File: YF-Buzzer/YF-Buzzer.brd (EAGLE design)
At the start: 100 x 100 mm, 40 parts, among them IC1 74HC595N, IC2 74HC595N, IC3 74HC595N, IC4 74HC595N, IC5 74HC595N, IC6 74HC595N, IC7 74150N

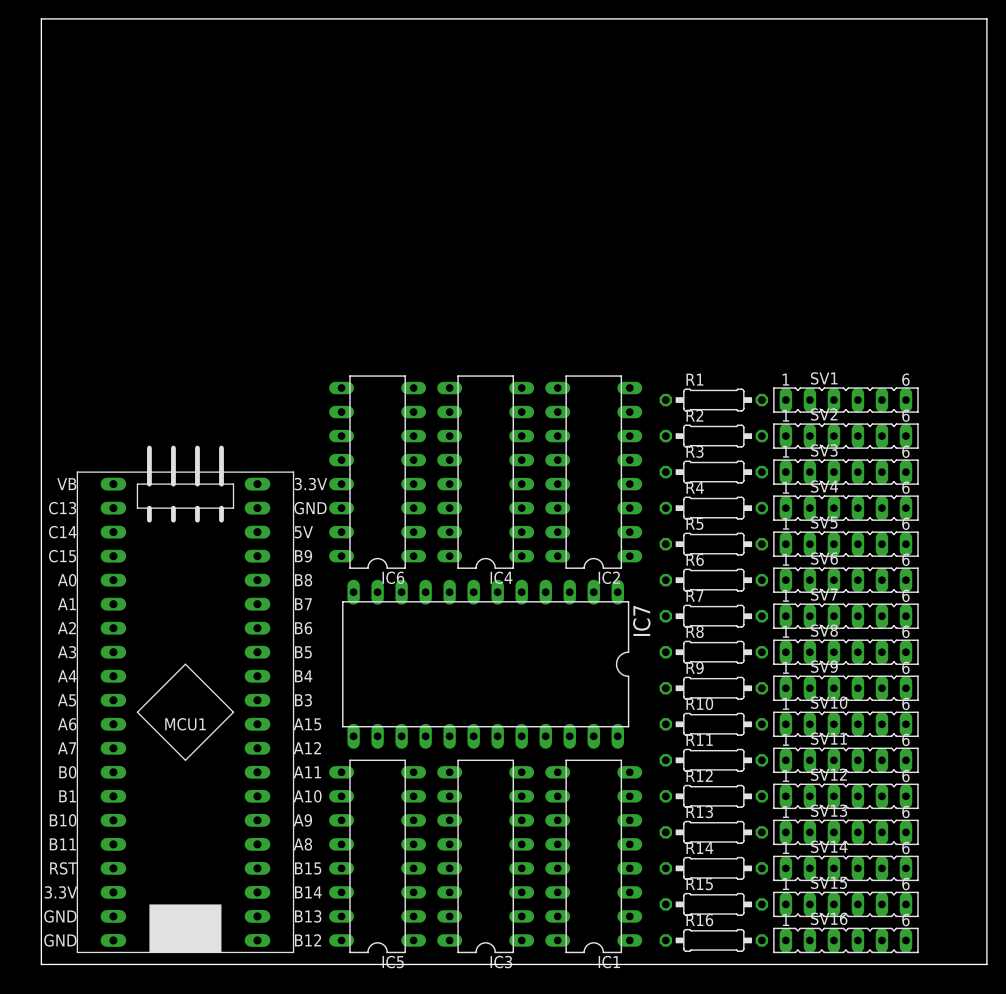
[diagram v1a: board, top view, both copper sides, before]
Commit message: Autorouted the rest of the main circuit.
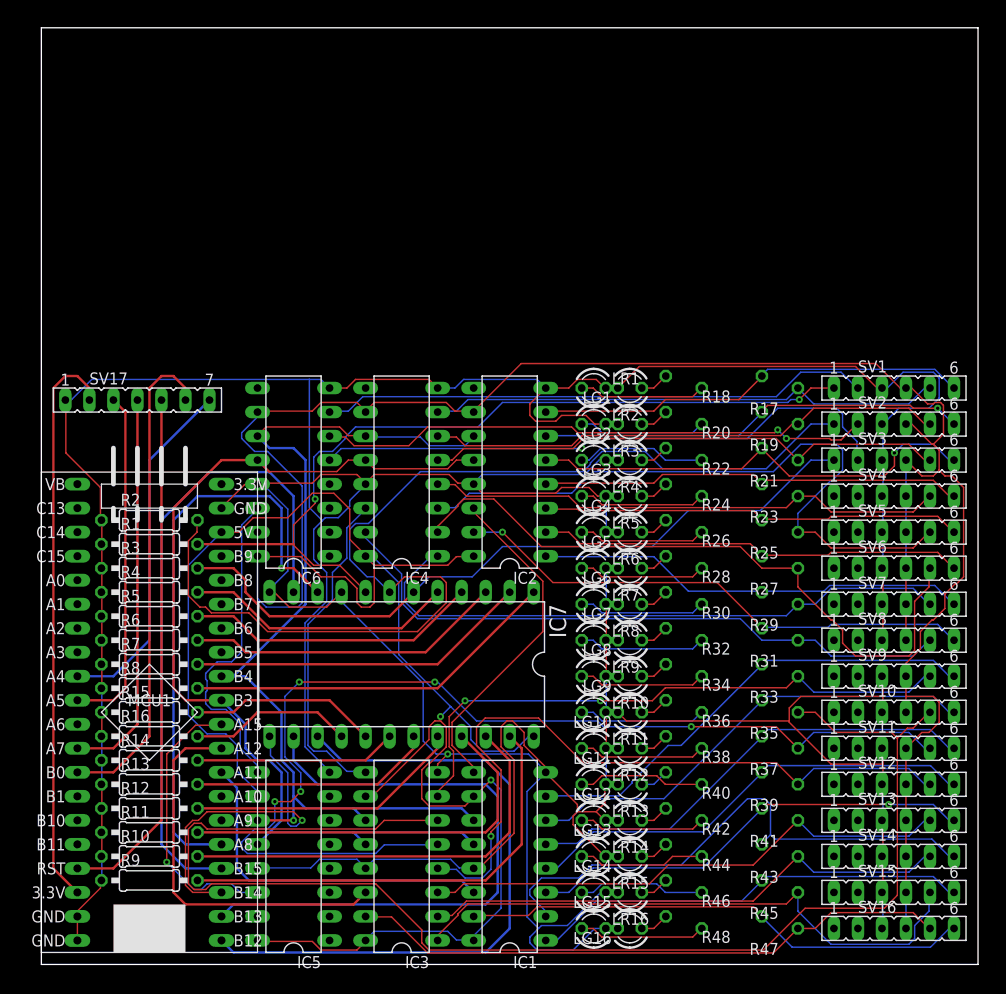
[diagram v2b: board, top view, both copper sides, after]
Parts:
- added LG1, LG10, LG11, LG12, LG13, LG14, LG15, LG16, LG2, LG3, LG4, LG5, LG6, LG7, LG8, LG9, LR1, LR10, LR11, LR12, LR13, LR14, LR15, LR16, LR2, LR3, LR4, LR5, LR6, LR7, LR8, LR9: (no value), led:LED3MM
- added R17, R18, R19, R20, R21, R22, R23, R24, R25, R26, R27, R28, R29, R30, R31, R32, R33, R34, R35, R36, R37, R38, R39, R40, R41, R42, R43, R44, R45, R46, R47, R48: (no value), rcl:0207/10
- added SV17: (no value), con-lsta:FE07
- moved R16 63.5 mm to (11.4, 24.1)
- moved R15 63.1 mm to (11.4, 26.7)
- moved R9 63.1 mm to (11.4, 8.89)
- moved R1 61.6 mm to (11.4, 44.5)
- moved R10 61.3 mm to (11.4, 11.4)
- moved R14 60.8 mm to (11.4, 21.6)
- moved R3 60.5 mm to (11.4, 41.9)
- moved R2 60.3 mm to (11.4, 47.0)
- moved R4 60.3 mm to (11.4, 39.4)
- moved R11 60.2 mm to (11.4, 14.0)
- moved R5 60.2 mm to (11.4, 36.8)
- moved R6 60.0 mm to (11.4, 34.3)
- moved R13 59.9 mm to (11.4, 19.1)
- moved R7 59.9 mm to (11.4, 31.8)
- moved R8 59.8 mm to (11.4, 29.2)
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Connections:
- removed net 3.3V1: MCU1.3.3V1
- new net LCD_CLK: MCU1.A5, SV17.3
- new net LCD_CS: MCU1.A4, SV17.7
- new net LCD_DATA: MCU1.A7, SV17.4
- new net LCD_DC: MCU1.B0, SV17.6
- new net LCD_RST: MCU1.R, SV17.5
- new net N$10: LG2.A, R20.1
- new net N$101: LR14.A, R43.1
- new net N$102: LG14.A, R44.1
- new net N$105: SV14.2
- new net N$106: SV14.1
- new net N$113: LR15.A, R45.1
- new net N$114: LG15.A, R46.1
- new net N$117: SV15.2
- new net N$118: SV15.1
- new net N$125: LR16.A, R47.1
- new net N$126: LG16.A, R48.1
- new net N$129: SV16.2
- new net N$130: SV16.1
- new net N$137: LR1.A, R17.1
- new net N$138: LG1.A, R18.1
- new net N$15: LR3.A, R21.1
- new net N$17: LG3.A, R22.1
- new net N$22: LR5.A, R25.1
- new net N$23: LG5.A, R26.1
- new net N$26: SV5.2
- new net N$27: SV5.1
- new net N$28: LR4.A, R23.1
- new net N$29: LG4.A, R24.1
- new net N$32: SV4.2
- new net N$33: SV4.1
- new net N$34: LR6.A, R27.1
- new net N$35: LG6.A, R28.1
- new net N$36: MCU1.3.3V1, SV17.2
- new net N$39: SV6.2
- new net N$40: SV6.1
- new net N$41: LR7.A, R29.1
- new net N$42: LG7.A, R30.1
- new net N$45: SV7.2
- new net N$46: SV7.1
- new net N$47: LR8.A, R31.1
- new net N$48: LG8.A, R32.1
- new net N$51: SV8.2
- new net N$52: SV8.1
- new net N$53: LR9.A, R33.1
- new net N$54: LG9.A, R34.1
- new net N$57: SV9.2
- new net N$58: SV9.1
- new net N$59: LR11.A, R37.1
- new net N$60: LG11.A, R38.1
- new net N$63: SV11.2
- new net N$64: SV11.1
- new net N$71: LR12.A, R39.1
- new net N$72: LG12.A, R40.1
- new net N$73: LR10.A, R35.1
- new net N$74: LG10.A, R36.1
- new net N$77: SV10.2
- new net N$78: SV10.1
- new net N$81: SV12.2
- new net N$82: SV12.1
- new net N$89: LR13.A, R41.1
- new net N$9: LR2.A, R19.1
- new net N$90: LG13.A, R42.1
- new net N$93: SV13.2
- new net N$94: SV13.1
- net IN10: no longer SV11.1
- net IN11: no longer SV12.1
- net IN12: no longer SV13.1
- net IN13: no longer SV14.1
- net IN14: no longer SV15.1
- net IN15: no longer SV16.1
- net IN3: no longer SV4.1
- net IN4: no longer SV5.1
- net IN5: no longer SV6.1
- net IN6: no longer SV7.1
- net IN7: no longer SV8.1
- net IN8: no longer SV9.1
- net IN9: no longer SV10.1
- net LG0: now also R18.2
- net LG1: now also R20.2
- net LG10: now also R38.2
- net LG11: now also R40.2
- net LG12: now also R42.2
- net LG13: now also R44.2
- net LG14: now also R46.2
- net LG15: now also R48.2
- net LG2: now also R22.2
- net LG3: now also R24.2
- net LG4: now also R26.2
- net LG5: now also R28.2
- net LG6: now also R30.2
- net LG7: now also R32.2
- net LG8: now also R34.2
- net LG9: now also R36.2
- net LR0: now also R17.2
- net LR1: now also R19.2
- net LR10: now also R37.2
- net LR11: now also R39.2
- net LR12: now also R41.2
- net LR13: now also R43.2
- net LR14: now also R45.2
- net LR15: now also R47.2
- net LR2: now also R21.2
- net LR3: now also R23.2
- net LR4: now also R25.2
- net LR5: now also R27.2
- net LR6: now also R29.2
- net LR7: now also R31.2
- net LR8: now also R33.2
- net LR9: now also R35.2
- net LY10: no longer SV11.2
- net LY11: no longer SV12.2
- net LY12: no longer SV13.2
- net LY13: no longer SV14.2
- net LY14: no longer SV15.2
- net LY15: no longer SV16.2
- net LY3: no longer SV4.2
- net LY4: no longer SV5.2
- net LY5: no longer SV6.2
- net LY6: no longer SV7.2
- net LY7: no longer SV8.2
- net LY8: no longer SV9.2
- net LY9: no longer SV10.2
- net PE: now also LG1.K, LG10.K, LG11.K, LG12.K, LG13.K, LG14.K, LG15.K, LG16.K, LG2.K, LG3.K, LG4.K, LG5.K, LG6.K, LG7.K, LG8.K, LG9.K, LR1.K, LR10.K, LR11.K, LR12.K, LR13.K, LR14.K, LR15.K, LR16.K, LR2.K, LR3.K, LR4.K, LR5.K, LR6.K, LR7.K, LR8.K, LR9.K, SV17.1
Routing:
- net PE: track 0.00 -> 594.3 mm, vias 0 -> 1
- net +5V: track 0.00 -> 401.9 mm, vias 0 -> 2
- net LR9: track 0.00 -> 147.5 mm
- net LR10: track 0.00 -> 115.6 mm, vias 0 -> 5
- net IN1: track 0.00 -> 113.8 mm
- net LATCH: track 0.00 -> 103.9 mm
- net CLK: track 0.00 -> 103.7 mm, vias 0 -> 1
- net IN0: track 0.00 -> 88.3 mm, vias 0 -> 2
- net IN2: track 0.00 -> 77.0 mm
- net LR11: track 0.00 -> 75.7 mm, vias 0 -> 1
- net LR4: track 0.00 -> 72.0 mm
- net LR5: track 0.00 -> 70.9 mm
- net MUX_A: track 0.00 -> 69.7 mm
- net MUX_D: track 0.00 -> 69.0 mm
- net LR7: track 0.00 -> 68.0 mm
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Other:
- board size 100 x 100 mm -> 99.1 x 99.1 mm

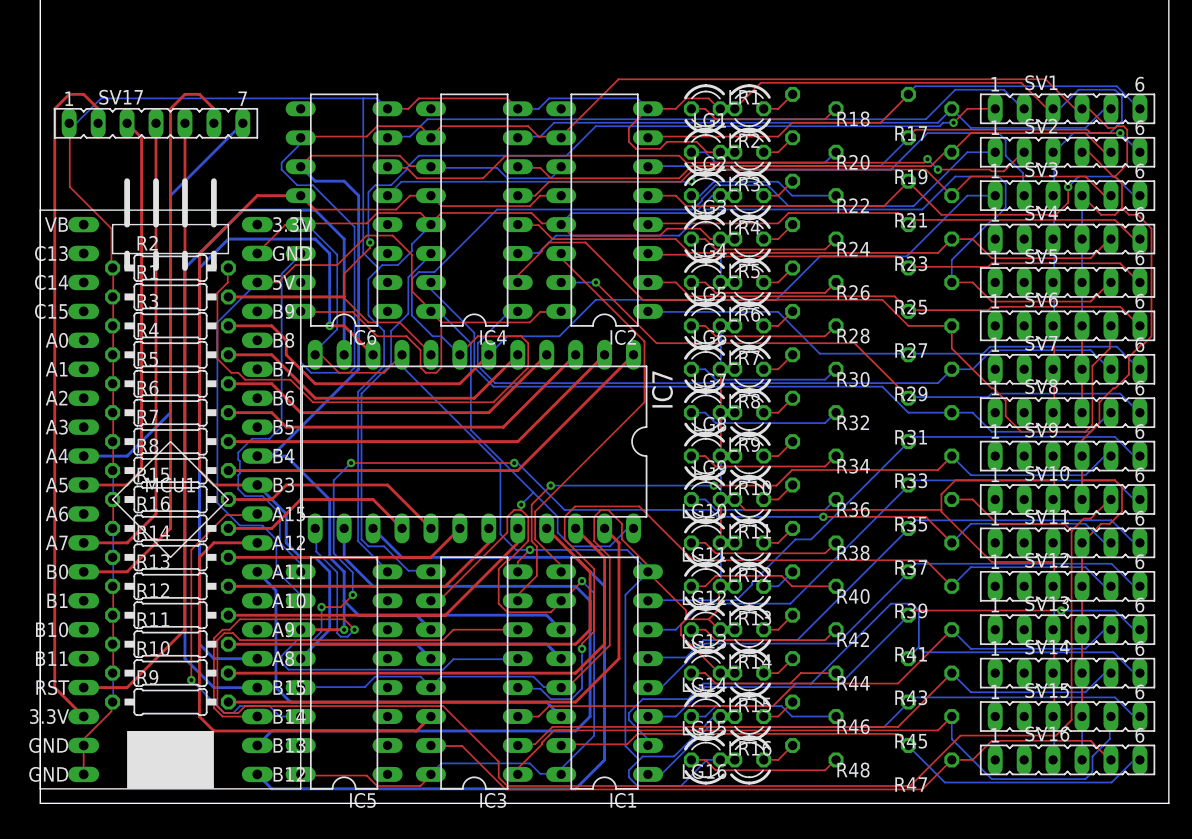
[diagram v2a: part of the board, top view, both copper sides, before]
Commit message: Removed LED's and cleaned up the circuit.
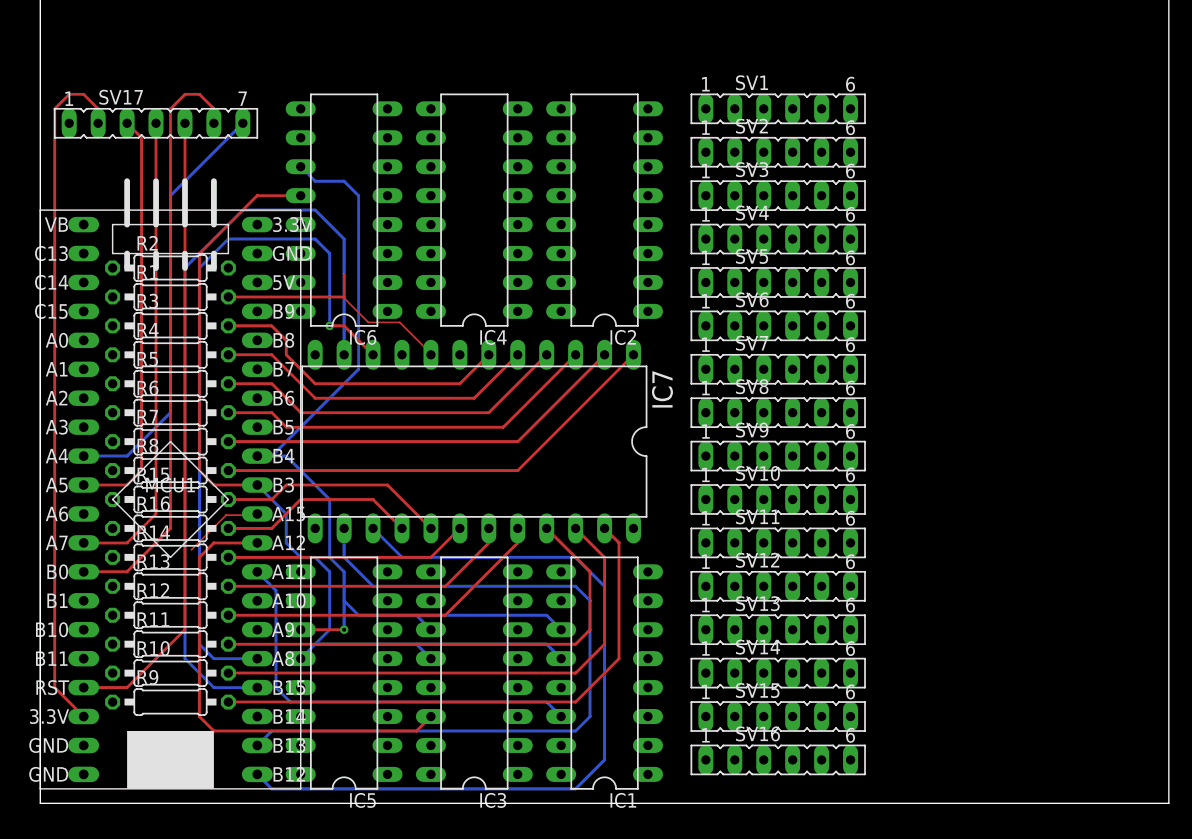
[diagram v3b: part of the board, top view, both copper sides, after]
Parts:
- removed LG1, LG10, LG11, LG12, LG13, LG14, LG15, LG16, LG2, LG3, LG4, LG5, LG6, LG7, LG8, LG9, LR1, LR10, LR11, LR12, LR13, LR14, LR15, LR16, LR2, LR3, LR4, LR5, LR6, LR7, LR8, LR9: (no value), led:LED3MM
- removed R17, R18, R19, R20, R21, R22, R23, R24, R25, R26, R27, R28, R29, R30, R31, R32, R33, R34, R35, R36, R37, R38, R39, R40, R41, R42, R43, R44, R45, R46, R47, R48: (no value), rcl:0207/10
- moved SV1 25.4 mm to (64.8, 61.0)
- moved SV10 25.4 mm to (64.8, 26.7)
- moved SV11 25.4 mm to (64.8, 22.9)
- moved SV12 25.4 mm to (64.8, 19.1)
- moved SV13 25.4 mm to (64.8, 15.2)
- moved SV14 25.4 mm to (64.8, 11.4)
- moved SV15 25.4 mm to (64.8, 7.62)
- moved SV16 25.4 mm to (64.8, 3.81)
- moved SV2 25.4 mm to (64.8, 57.1)
- moved SV3 25.4 mm to (64.8, 53.3)
- moved SV4 25.4 mm to (64.8, 49.5)
- moved SV5 25.4 mm to (64.8, 45.7)
- moved SV6 25.4 mm to (64.8, 41.9)
- moved SV7 25.4 mm to (64.8, 38.1)
- moved SV8 25.4 mm to (64.8, 34.3)
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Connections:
- removed net N$10: LG2.A, R20.1
- removed net N$101: LR14.A, R43.1
- removed net N$102: LG14.A, R44.1
- removed net N$105: SV14.2
- removed net N$106: SV14.1
- removed net N$113: LR15.A, R45.1
- removed net N$114: LG15.A, R46.1
- removed net N$117: SV15.2
- removed net N$118: SV15.1
- removed net N$125: LR16.A, R47.1
- removed net N$126: LG16.A, R48.1
- removed net N$129: SV16.2
- removed net N$130: SV16.1
- removed net N$137: LR1.A, R17.1
- removed net N$138: LG1.A, R18.1
- removed net N$15: LR3.A, R21.1
- removed net N$17: LG3.A, R22.1
- removed net N$22: LR5.A, R25.1
- removed net N$23: LG5.A, R26.1
- removed net N$26: SV5.2
- removed net N$27: SV5.1
- removed net N$28: LR4.A, R23.1
- removed net N$29: LG4.A, R24.1
- removed net N$32: SV4.2
- removed net N$33: SV4.1
- removed net N$34: LR6.A, R27.1
- removed net N$35: LG6.A, R28.1
- removed net N$39: SV6.2
- removed net N$40: SV6.1
- removed net N$41: LR7.A, R29.1
- removed net N$42: LG7.A, R30.1
- removed net N$45: SV7.2
- removed net N$46: SV7.1
- removed net N$47: LR8.A, R31.1
- removed net N$48: LG8.A, R32.1
- removed net N$51: SV8.2
- removed net N$52: SV8.1
- removed net N$53: LR9.A, R33.1
- removed net N$54: LG9.A, R34.1
- removed net N$57: SV9.2
- removed net N$58: SV9.1
- removed net N$59: LR11.A, R37.1
- removed net N$60: LG11.A, R38.1
- removed net N$63: SV11.2
- removed net N$64: SV11.1
- removed net N$71: LR12.A, R39.1
- removed net N$72: LG12.A, R40.1
- removed net N$73: LR10.A, R35.1
- removed net N$74: LG10.A, R36.1
- removed net N$77: SV10.2
- removed net N$78: SV10.1
- removed net N$81: SV12.2
- removed net N$82: SV12.1
- removed net N$89: LR13.A, R41.1
- removed net N$9: LR2.A, R19.1
- removed net N$90: LG13.A, R42.1
- removed net N$93: SV13.2
- removed net N$94: SV13.1
- net IN10: now also SV11.1
- net IN11: now also SV12.1
- net IN12: now also SV13.1
- net IN13: now also SV14.1
- net IN14: now also SV15.1
- net IN15: now also SV16.1
- net IN3: now also SV4.1
- net IN4: now also SV5.1
- net IN5: now also SV6.1
- net IN6: now also SV7.1
- net IN7: now also SV8.1
- net IN8: now also SV9.1
- net IN9: now also SV10.1
- net LG0: no longer R18.2
- net LG1: no longer R20.2
- net LG10: no longer R38.2
- net LG11: no longer R40.2
- net LG12: no longer R42.2
- net LG13: no longer R44.2
- net LG14: no longer R46.2
- net LG15: no longer R48.2
- net LG2: no longer R22.2
- net LG3: no longer R24.2
- net LG4: no longer R26.2
- net LG5: no longer R28.2
- net LG6: no longer R30.2
- net LG7: no longer R32.2
- net LG8: no longer R34.2
- net LG9: no longer R36.2
- net LR0: no longer R17.2
- net LR1: no longer R19.2
- net LR10: no longer R37.2
- net LR11: no longer R39.2
- net LR12: no longer R41.2
- net LR13: no longer R43.2
- net LR14: no longer R45.2
- net LR15: no longer R47.2
- net LR2: no longer R21.2
- net LR3: no longer R23.2
- net LR4: no longer R25.2
- net LR5: no longer R27.2
- net LR6: no longer R29.2
- net LR7: no longer R31.2
- net LR8: no longer R33.2
- net LR9: no longer R35.2
- net LY10: now also SV11.2
- net LY11: now also SV12.2
- net LY12: now also SV13.2
- net LY13: now also SV14.2
- net LY14: now also SV15.2
- net LY15: now also SV16.2
- net LY3: now also SV4.2
- net LY4: now also SV5.2
- net LY5: now also SV6.2
- net LY6: now also SV7.2
- net LY7: now also SV8.2
- net LY8: now also SV9.2
- net LY9: now also SV10.2
- net PE: no longer LG1.K, LG10.K, LG11.K, LG12.K, LG13.K, LG14.K, LG15.K, LG16.K, LG2.K, LG3.K, LG4.K, LG5.K, LG6.K, LG7.K, LG8.K, LG9.K, LR1.K, LR10.K, LR11.K, LR12.K, LR13.K, LR14.K, LR15.K, LR16.K, LR2.K, LR3.K, LR4.K, LR5.K, LR6.K, LR7.K, LR8.K, LR9.K
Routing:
- net PE: track 594.3 -> 0.00 mm, vias 1 -> 0
- net +5V: track 401.9 -> 0.00 mm, vias 2 -> 0
- net LR9: track 147.5 -> 0.00 mm
- net LR10: track 115.6 -> 0.05 mm, vias 5 -> 0
- net IN1: track 113.8 -> 0.00 mm
- net LR11: track 75.7 -> 0.00 mm, vias 1 -> 0
- net LR4: track 72.0 -> 0.00 mm
- net LR5: track 70.9 -> 0.00 mm
- net LR7: track 68.0 -> 0.00 mm
- net IN0: track 88.3 -> 22.0 mm, vias 2 -> 0
- net LR6: track 64.8 -> 0.00 mm
- net LR15: track 63.8 -> 0.00 mm
- net LR8: track 63.3 -> 0.00 mm, vias 2 -> 0
- net LY2: track 62.5 -> 0.00 mm, vias 1 -> 0
- net LR14: track 62.2 -> 0.00 mm
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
